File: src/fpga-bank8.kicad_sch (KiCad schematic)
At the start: 1 part

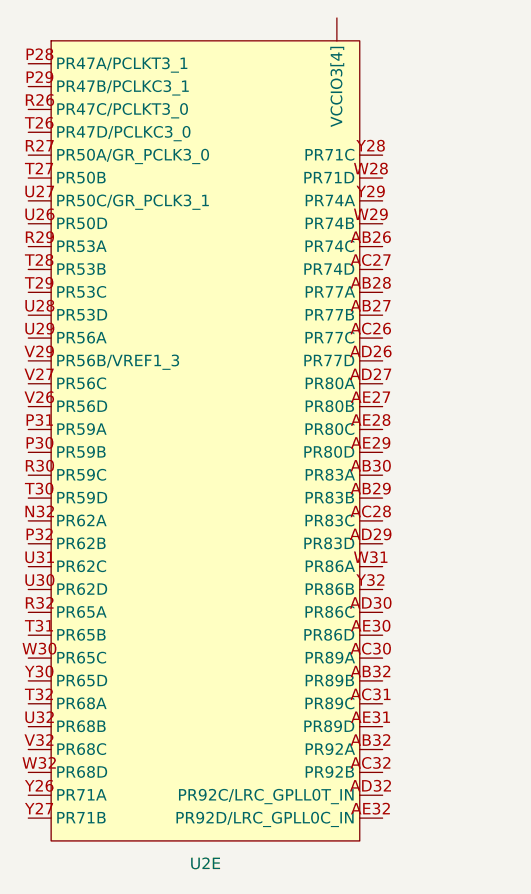
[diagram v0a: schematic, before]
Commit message: Finishes FPGA symbol
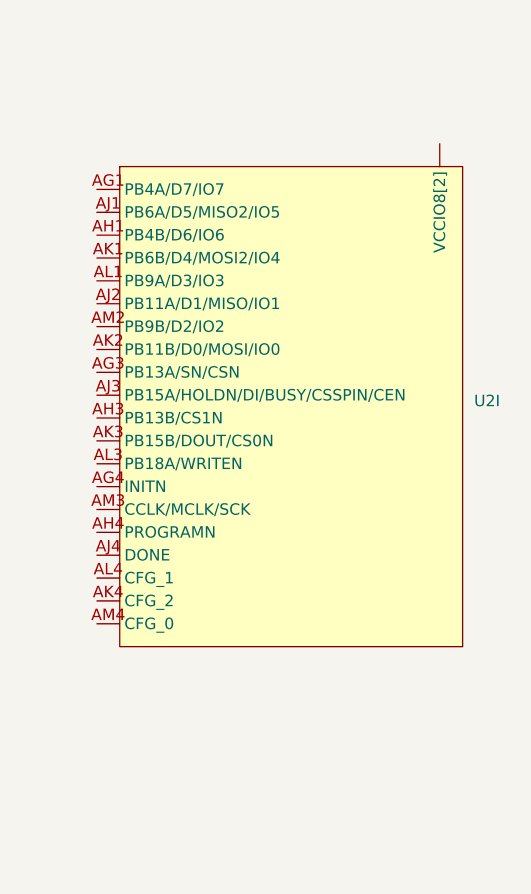
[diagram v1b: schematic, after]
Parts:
- removed U2: ~, symbol ECAP5-BSOM:LFE5U-85F-*BG756*
- added U2: ~, symbol ECAP5-BSOM:LFE5U-85F-*BG756*
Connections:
- new net VCCIO8: U2. (VCCIO8[2]), U2.AB10 (VCCIO8), U2.AC10 (VCCIO8)

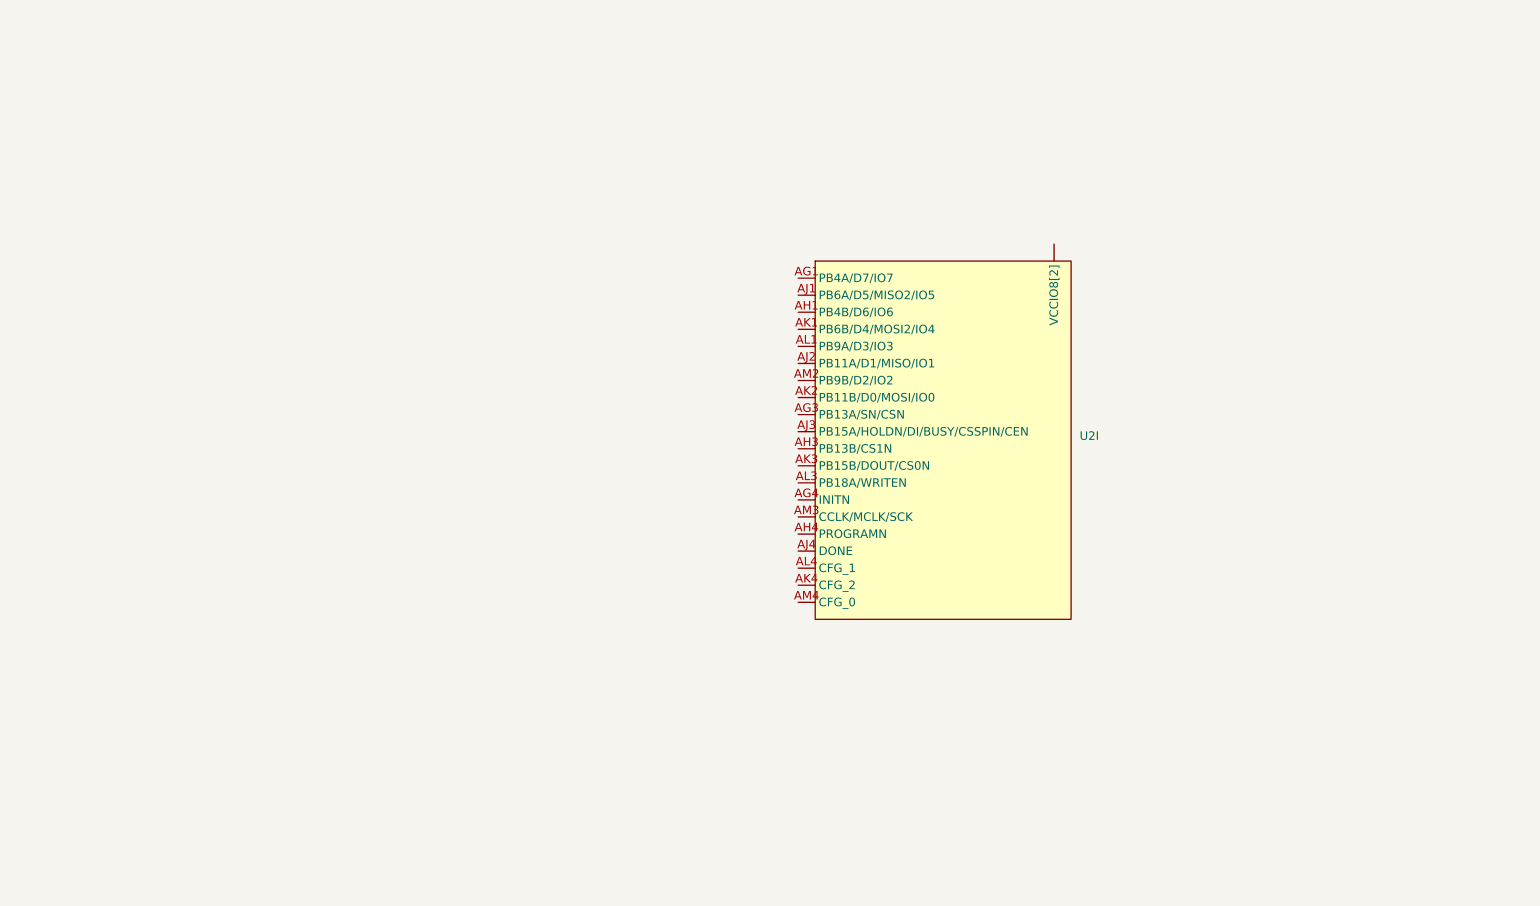
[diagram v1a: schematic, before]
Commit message: Updates the fpga configuration schematic
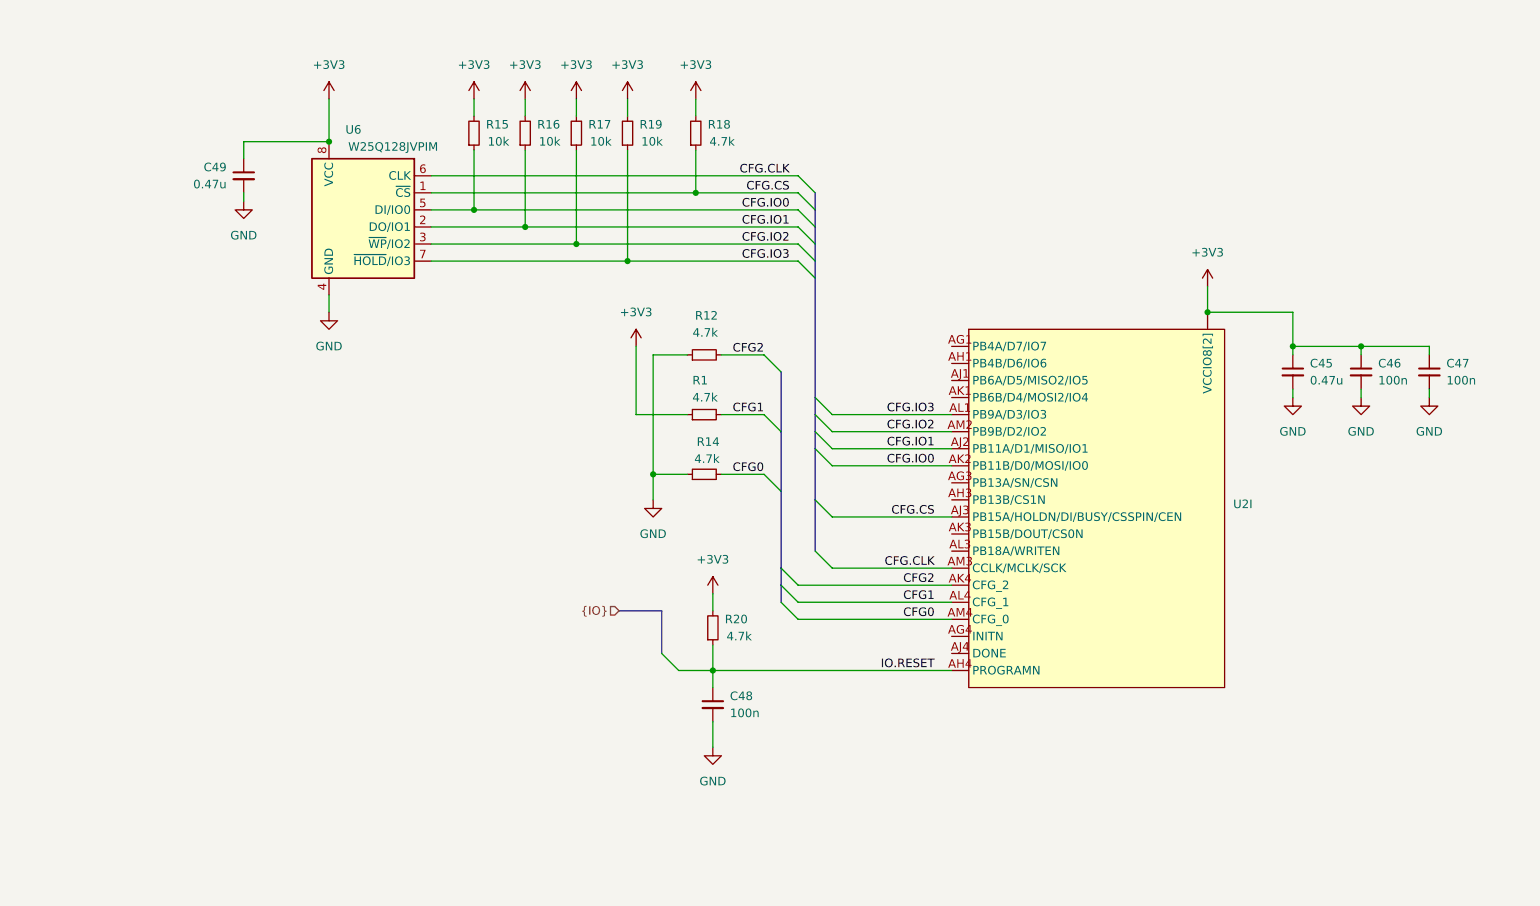
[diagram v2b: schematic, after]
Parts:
- added C45, C49: 0.47u, symbol Device:C_Small
- added C46, C47, C48: 100n, symbol Device:C_Small
- added R1, R12, R14, R18, R20: 4.7k, symbol Device:R_Small
- added R15, R16, R17, R19: 10k, symbol Device:R_Small
- added U6: W25Q128JVPIM, symbol ECAP5-BSOM:W25Q128JVPIM
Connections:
- net IO.RESET: now reaches U2.AH4 (PROGRAMN)
- net IO.RESET: now also C48.1, R20.1
- net CFG.IO1: now reaches U2.AJ2 (PB11A/D1/MISO/IO1)
- net CFG.IO1: now also R16.1, U6.2 (DO/IO1)
- net CFG.CS: now reaches U2.AJ3 (PB15A/HOLDN/DI/BUSY/CSSPIN/CEN)
- net CFG.CS: now also R18.1, U6.1 (~{CS})
- net CFG.IO0: now reaches U2.AK2 (PB11B/D0/MOSI/IO0)
- net CFG.IO0: now also R15.1, U6.5 (DI/IO0)
- net CFG2: now reaches U2.AK4 (CFG_2)
- net CFG2: now also R12.2
- net CFG.IO3: now reaches U2.AL1 (PB9A/D3/IO3)
- net CFG.IO3: now also R19.1, U6.7 (~{HOLD}/IO3)
- net CFG1: now reaches U2.AL4 (CFG_1)
- net CFG1: now also R1.2
- net CFG.IO2: now reaches U2.AM2 (PB9B/D2/IO2)
- net CFG.IO2: now also R17.1, U6.3 (~{WP}/IO2)
- net CFG.CLK: now reaches U2.AM3 (CCLK/MCLK/SCK)
- net CFG.CLK: now also U6.6 (CLK)
- net CFG0: now reaches U2.AM4 (CFG_0)
- net CFG0: now also R14.2
- net VCCIO8 renamed +3V3
- net +3V3: now also C45.1, C46.1, C47.1, C49.1, R1.1, R15.2, R16.2, R17.2, R18.2, R19.2, R20.2, U6.8 (VCC)
- new net GND: C45.2, C46.2, C47.2, C48.2, C49.2, R12.1, R14.1, U6.4 (GND)
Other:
- moved on the sheet: U2I

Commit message: Adds SRAM symbol
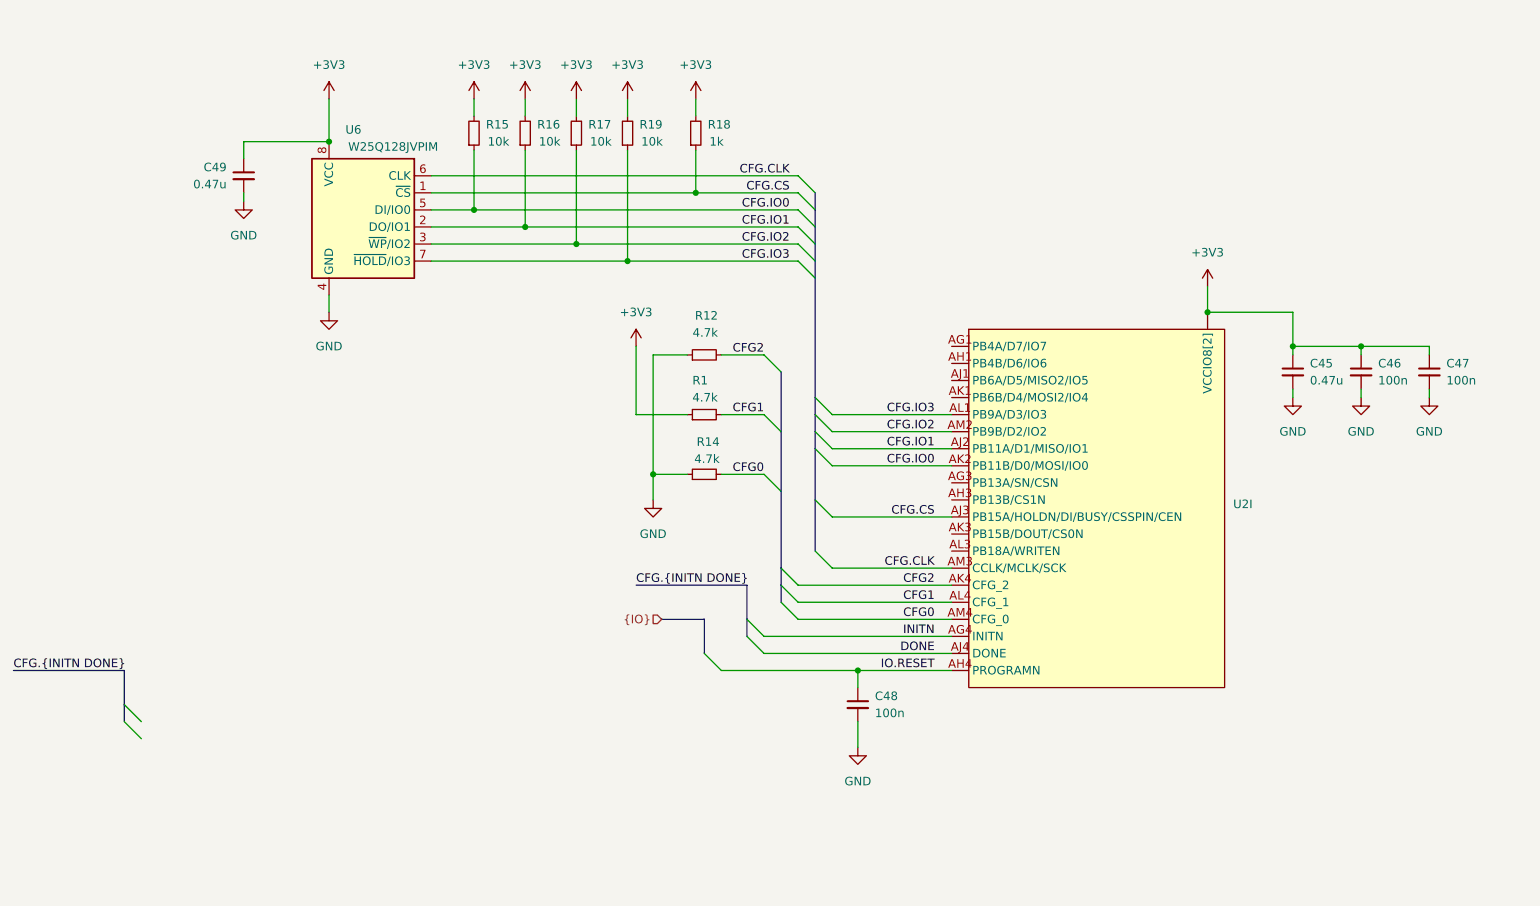
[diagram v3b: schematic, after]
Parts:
- removed R20: 4.7k, symbol Device:R_Small
- R18: value 4.7k -> 1k
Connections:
- net INITN: now reaches U2.AG4 (INITN)
- net DONE: now reaches U2.AJ4 (DONE)
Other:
- moved on the sheet: C48

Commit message: Finishes the configuration schematic
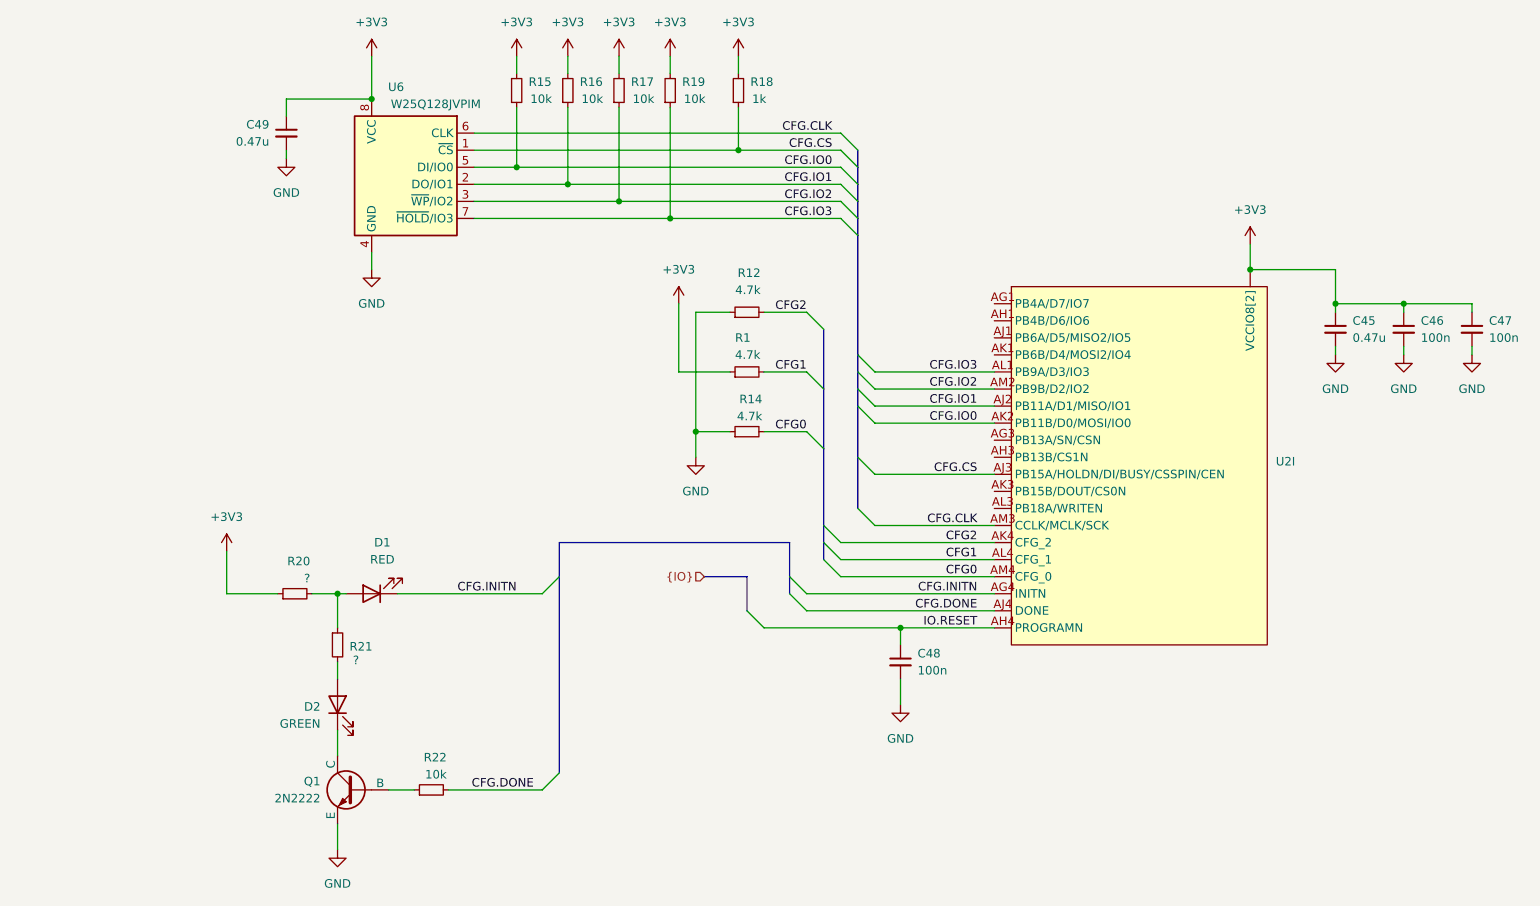
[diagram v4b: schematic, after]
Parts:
- added D1: RED, symbol Device:LED
- added D2: GREEN, symbol Device:LED
- added Q1: 2N2222, symbol Simulation_SPICE:NPN
- added R20, R21: ?, symbol Device:R_Small
- added R22: 10k, symbol Device:R_Small
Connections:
- net +3V3: now also R20.1
- net GND: now also Q1.3 (E)
- net DONE renamed CFG.DONE
- net CFG.DONE: now also R22.2
- net INITN renamed CFG.INITN
- net CFG.INITN: now also D1.1 (K)
- new net: D1.2 (A), R20.2, R21.1
- new net: D2.2 (A), R21.2
- new net: D2.1 (K), Q1.1 (C)
- new net: Q1.2 (B), R22.1
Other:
- moved on the sheet: C45, C46, C47, C48, C49, R1, R12, R14, R15, R16, R17, R18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

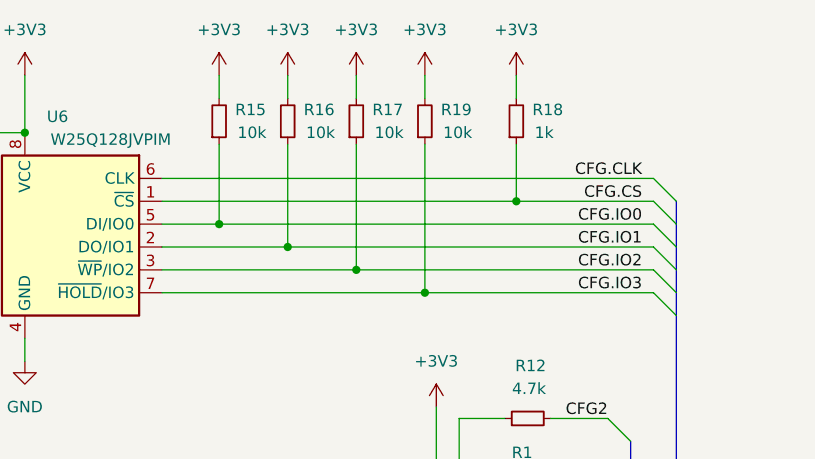
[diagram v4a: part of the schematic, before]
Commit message: Adds DDR symbol
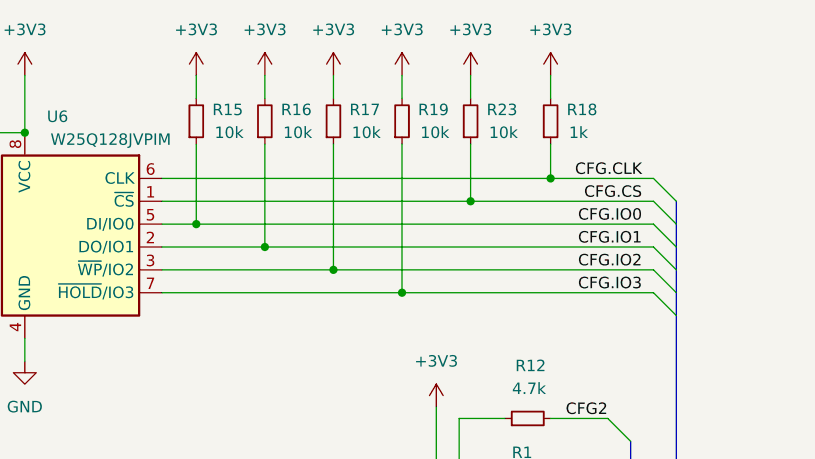
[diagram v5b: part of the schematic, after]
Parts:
- added R23: 10k, symbol Device:R_Small
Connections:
- net +3V3: now also R23.2
- net CFG.CLK: now also R18.1
- net CFG.CS: now also R23.1; no longer R18.1
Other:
- moved on the sheet: R15, R16, R17, R18, R19
